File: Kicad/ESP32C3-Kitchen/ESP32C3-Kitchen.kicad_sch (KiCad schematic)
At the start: 27 parts, among them Q1 BTA24-800B, Q2 BTA24-800B, Q3 BTA24-800B, U1 MOC3041M, U2 MOC3041M, U3 MOC3041M, U4 HLK-5M05

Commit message: Kicad: Details
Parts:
- added D1: LED_KRGB, symbol Device:LED_KRGB
- added R13, R14, R15: 150, symbol Device:R
- C1, C2, C3, R12, R3, R8: now not fitted
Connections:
- net GNDD: now also D1.1 (K)
- new net: D1.4 (BA), R15.1
- new net: D1.3 (GA), R14.1
- new net: D1.2 (RA), R13.1
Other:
- moved on the sheet: C4, C5, F1, L1, Q1, Q2, Q3, R1, R10, R11, R2, R4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

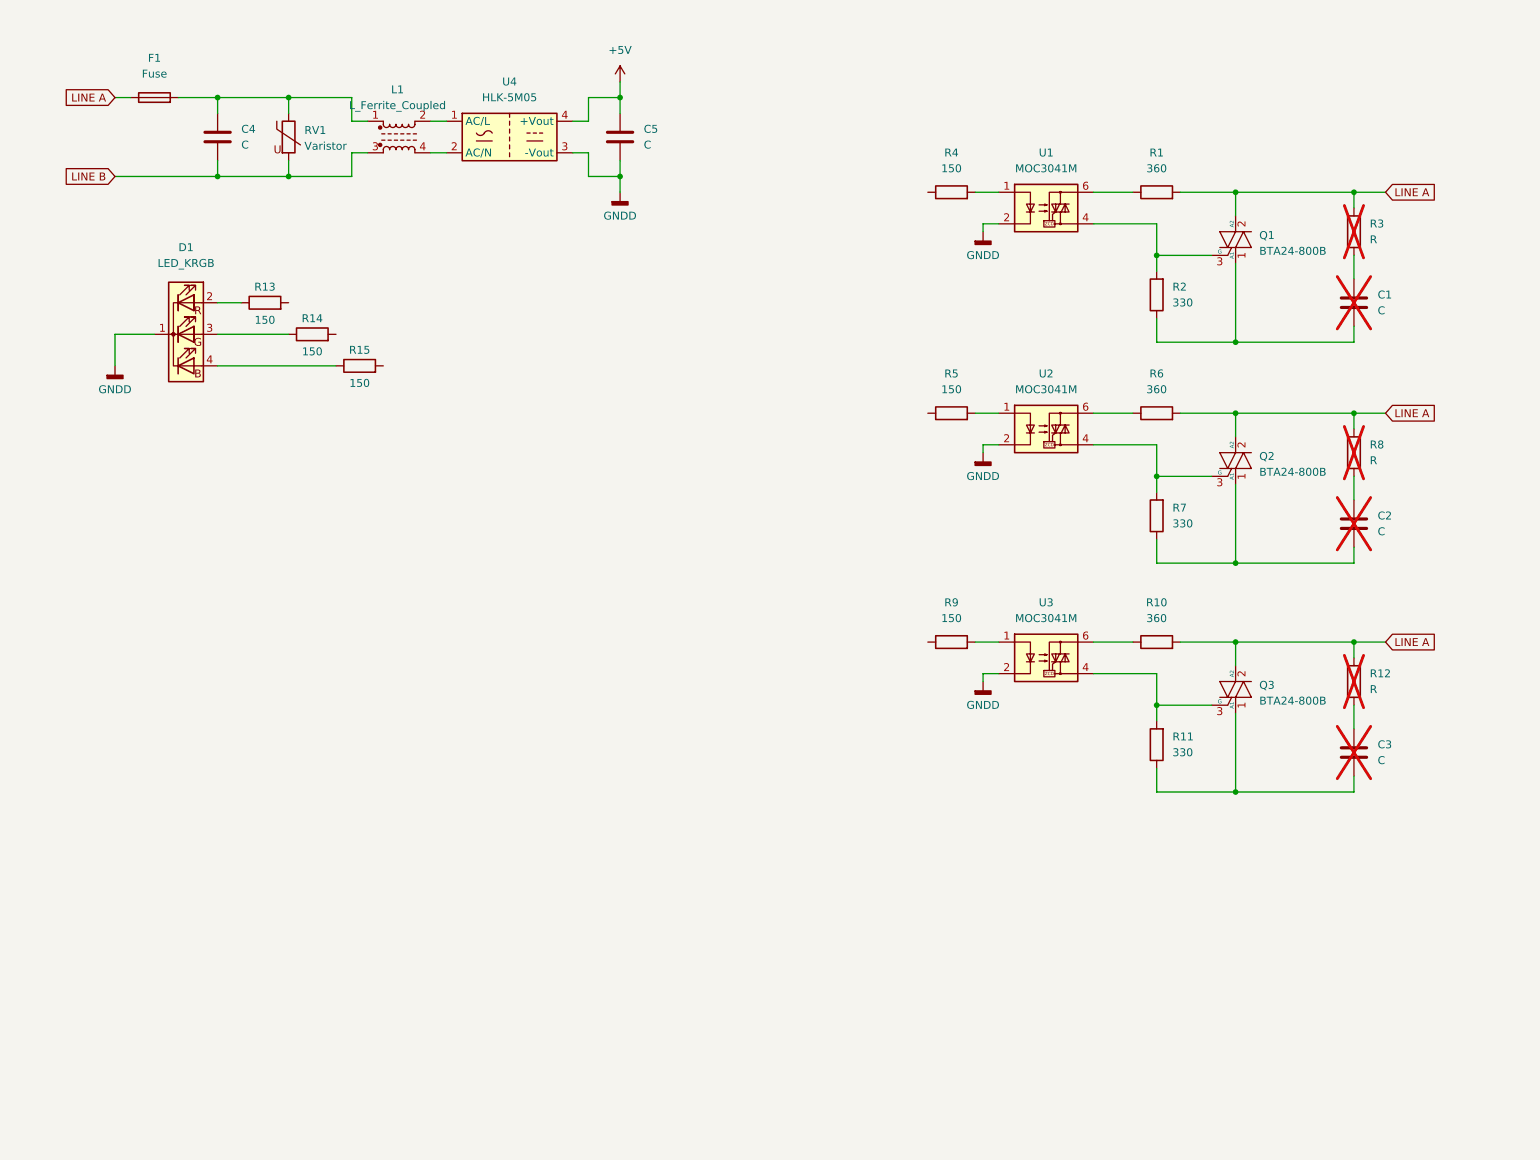
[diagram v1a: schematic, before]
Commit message: Kicad: Terminal blocks, footprints, values, sheet style...
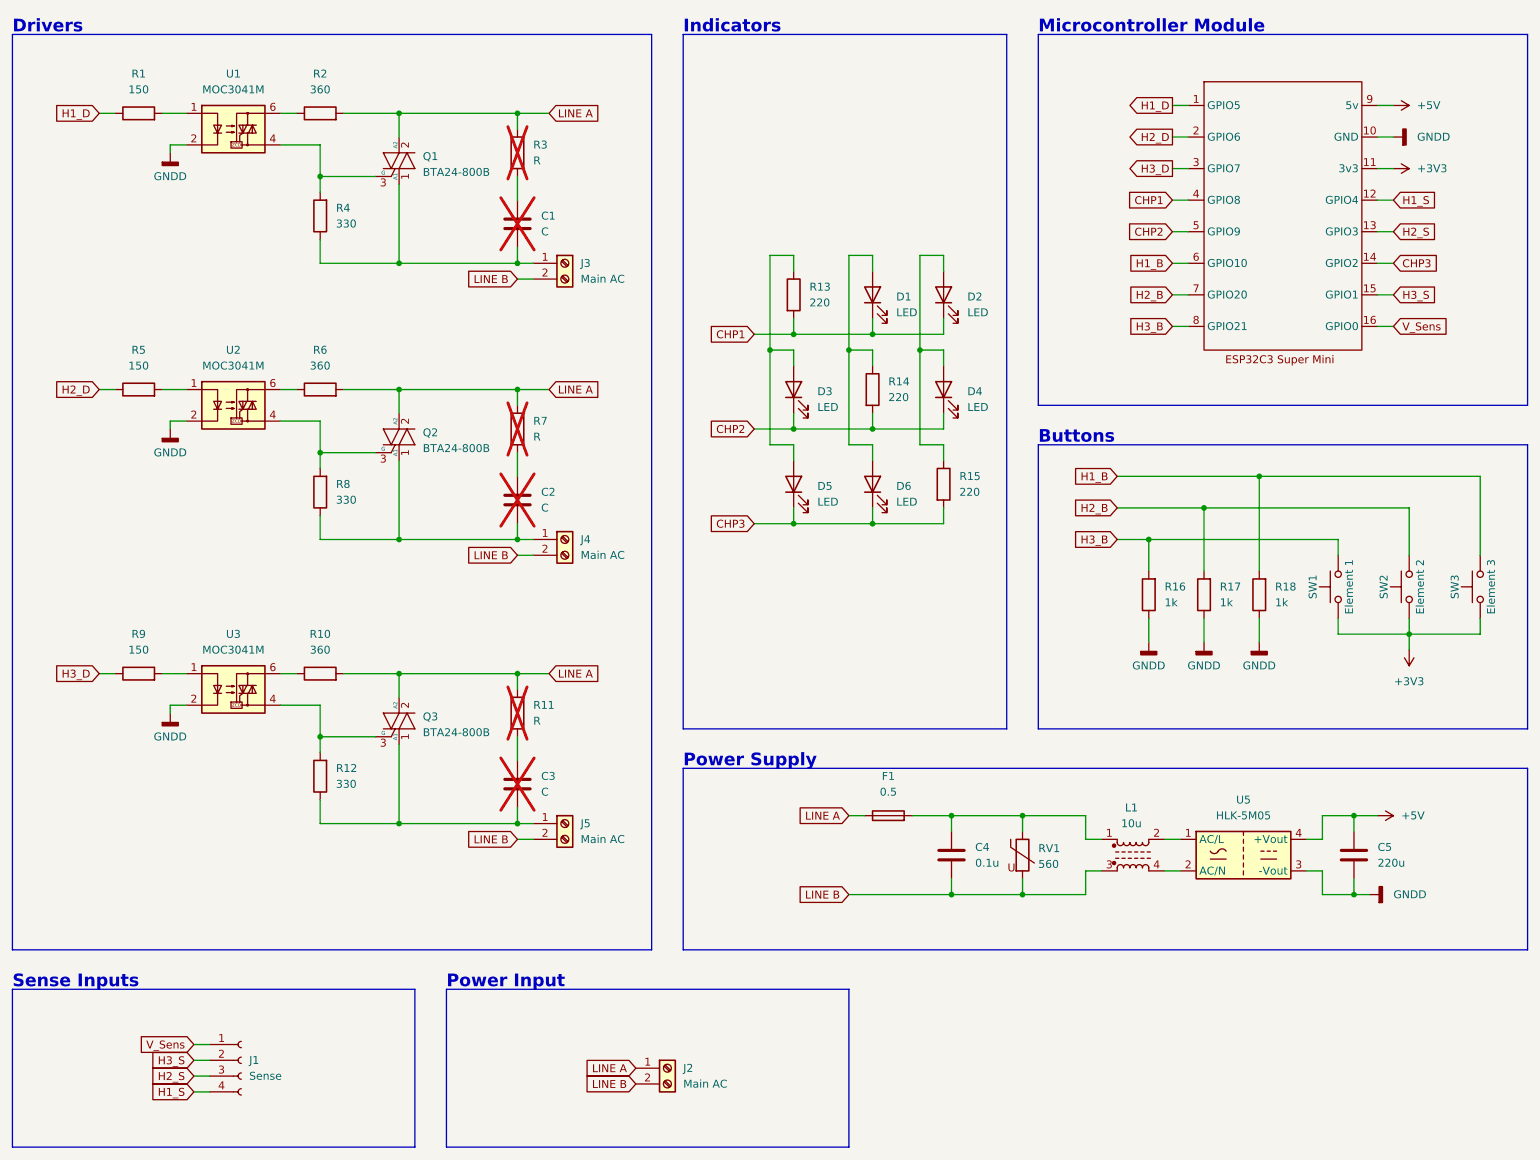
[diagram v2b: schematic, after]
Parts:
- removed D1: LED_KRGB, symbol Device:LED_KRGB
- added D1, D2, D3, D4, D5, D6: LED, LED_THT:LED_D3.0mm, symbol Device:LED
- added J1: Sense, Connector_PinHeader_2.54mm:PinHeader_1x04_P2.54mm_Vertical, symbol Connector:Conn_01x04_Socket
- added J2, J3, J4, J5: Main AC, TerminalBlock_Phoenix:TerminalBlock_Phoenix_MKDS-1,5-2-5.08_1x02_P5.08mm_Horizontal, symbol Connector:Screw_Terminal_01x02
- added R16, R17, R18: 1k, Resistor_SMD:R_1206_3216Metric_Pad1.30x1.75mm_HandSolder, symbol Device:R
- added SW1: Element 1, Button_Switch_THT:SW_PUSH_6mm, symbol Switch:SW_Push
- added SW2: Element 2, Button_Switch_THT:SW_PUSH_6mm, symbol Switch:SW_Push
- added SW3: Element 3, Button_Switch_THT:SW_PUSH_6mm, symbol Switch:SW_Push
- added U4: (no value), Modules:ESP32C3-SM, symbol Modules:ESP32C3_SM
- C4: value C -> 0.1u; footprint (none) -> Capacitor_THT:C_Disc_D10.0mm_W2.5mm_P5.00mm
- C5: value C -> 220u; footprint (none) -> Capacitor_THT:C_Radial_D10.0mm_H12.5mm_P5.00mm
- F1: value Fuse -> 0.5; footprint (none) -> Fuse:Fuse_Littelfuse_395Series
- L1: value L_Ferrite_Coupled -> 10u; footprint (none) -> Inductor_THT:L_CommonMode_PulseElectronics_PH9455x105NL_1
- R1: renamed from R4; footprint (none) -> Resistor_SMD:R_1206_3216Metric_Pad1.30x1.75mm_HandSolder
- R10, R6: footprint (none) -> Resistor_THT:R_Axial_DIN0309_L9.0mm_D3.2mm_P15.24mm_Horizontal
- R11, R7: value 330 -> R; now not fitted
- R12, R8: value R -> 330; footprint (none) -> Resistor_THT:R_Axial_DIN0309_L9.0mm_D3.2mm_P15.24mm_Horizontal; now fitted
- R13, R14, R15: value 150 -> 220; footprint (none) -> Resistor_SMD:R_1206_3216Metric_Pad1.30x1.75mm_HandSolder
- R2: renamed from R1; footprint (none) -> Resistor_THT:R_Axial_DIN0309_L9.0mm_D3.2mm_P15.24mm_Horizontal
- R4: renamed from R2; footprint (none) -> Resistor_THT:R_Axial_DIN0309_L9.0mm_D3.2mm_P15.24mm_Horizontal
- R5, R9: footprint (none) -> Resistor_SMD:R_1206_3216Metric_Pad1.30x1.75mm_HandSolder
- RV1: value Varistor -> 560; footprint (none) -> Varistor:RV_Disc_D7mm_W3.4mm_P5mm
- U1, U2, U3: footprint (none) -> Package_DIP:DIP-6_W7.62mm_LongPads
- renumbered U4 to U5
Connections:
- net +5V: now also U4.9 (5v)
- net GNDD: now also R16.1, R17.1, R18.1, U4.10 (GND)
- net LINE A: now also R11.2, R7.2, J2.1 (Pin_1); no longer R12.2, R8.2
- net LINE B: now also J2.2 (Pin_2), J3.2 (Pin_2), J4.2 (Pin_2), J5.2 (Pin_2)
- net H1_D: now reaches R1.1
- net H1_D: now also U4.1 (GPIO5)
- net at C1.2, Q1.1 (A1), R4.1: now also J3.1 (Pin_1)
- net H2_D: now reaches R5.1
- net H2_D: now also U4.2 (GPIO6)
- net at C2.2, Q2.1 (A1): now also R8.1, J4.1 (Pin_1); no longer R7.1
- net at Q2.3 (G), U2.4: now also R8.2; no longer R7.2
- net at C3.2, Q3.1 (A1): now also R12.1, J5.1 (Pin_1); no longer R11.1
- net at Q3.3 (G), U3.4: now also R12.2; no longer R11.2
- net at R15.1: now also D2.2 (A), D4.2 (A)
- net CHP3: now reaches R15.2
- net CHP3: now also D5.1 (K), D6.1 (K), U4.14 (GPIO2)
- net at C3.1: now also R11.1; no longer R12.1
- net at R14.1: now also D1.2 (A), D6.2 (A)
- net CHP2: now reaches R14.2
- net CHP2: now also D3.1 (K), D4.1 (K), U4.5 (GPIO9)
- net at R13.1: now also D3.2 (A), D5.2 (A)
- net at C2.1: now also R7.1; no longer R8.1
- net H3_D: now reaches R9.1
- net H3_D: now also U4.3 (GPIO7)
- net CHP1: now reaches R13.2
- net CHP1: now also D1.1 (K), D2.1 (K), U4.4 (GPIO8)
- new net +3V3: SW1.1, SW2.1, SW3.1, U4.11 (3v3)
- new net H1_B: R18.2, SW3.2, U4.6 (GPIO10)
- new net H1_S: J1.4 (Pin_4), U4.12 (GPIO4)
- new net H2_B: R17.2, SW2.2, U4.7 (GPIO20)
- new net H2_S: J1.3 (Pin_3), U4.13 (GPIO3)
- new net H3_B: R16.2, SW1.2, U4.8 (GPIO21)
- new net H3_S: J1.2 (Pin_2), U4.15 (GPIO1)
- new net V_Sens: J1.1 (Pin_1), U4.16 (GPIO0)
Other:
- note added: "Buttons"
- note added: "Drivers"
- note added: "Indicators"
- note added: "Microcontroller Module"
- note added: "Power Input"
- note added: "Power Supply"
- note added: "Sense Inputs"
- moved on the sheet: C1, C4, C5, F1, L1, Q1, R1, R2, R3, R4, RV1, U1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

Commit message: Kicad: Finish one layer version schematic and PCB
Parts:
- added J6: Voltage Output, Connector_PinHeader_2.54mm:PinHeader_1x03_P2.54mm_Vertical, symbol Connector:Conn_01x03_Pin
- L1: footprint Inductor_THT:L_CommonMode_PulseElectronics_PH9455x105NL_1 -> Inductor_THT:Choke_Schaffner_RN212-04-12.5x18.0mm
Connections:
- net +3V3: now also J6.3 (Pin_3)
- net +5V: now also J6.1 (Pin_1)
- net CHP1: now also U4.14 (GPIO2); no longer U4.4 (GPIO8)
- net CHP3: now also U4.4 (GPIO8); no longer U4.14 (GPIO2)
- net GNDD: now also J6.2 (Pin_2)
- net LINE A: now also C4.2, L1.4, RV1.2; no longer F1.1
- net LINE B: now also F1.1; no longer C4.2, L1.3, RV1.2
- net at C4.1, F1.2, RV1.1: now also L1.2; no longer L1.1
- net at U5.1 (AC/L): now also L1.1; no longer L1.2
- net at U5.2 (AC/N): now also L1.3; no longer L1.4
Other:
- note added: "Power Output"
- moved on the sheet: J1, J2
